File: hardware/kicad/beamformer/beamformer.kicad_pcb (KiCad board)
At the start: 2 copper layers, 96 parts, among them J1 SWD_HEADER, J2 USB_C_Receptacle_USB2.0_16P, U1 STM32H753ZITx, U2 USBLC6-2SC6, U3 TLC59116FIPWR, U4 ADAU7118ACPZRL, U5 MCP1826S-3302E/DB, U6 TLV75518PDBVR, U7 SN74AXC4T774PWR, Y1 16 MHz

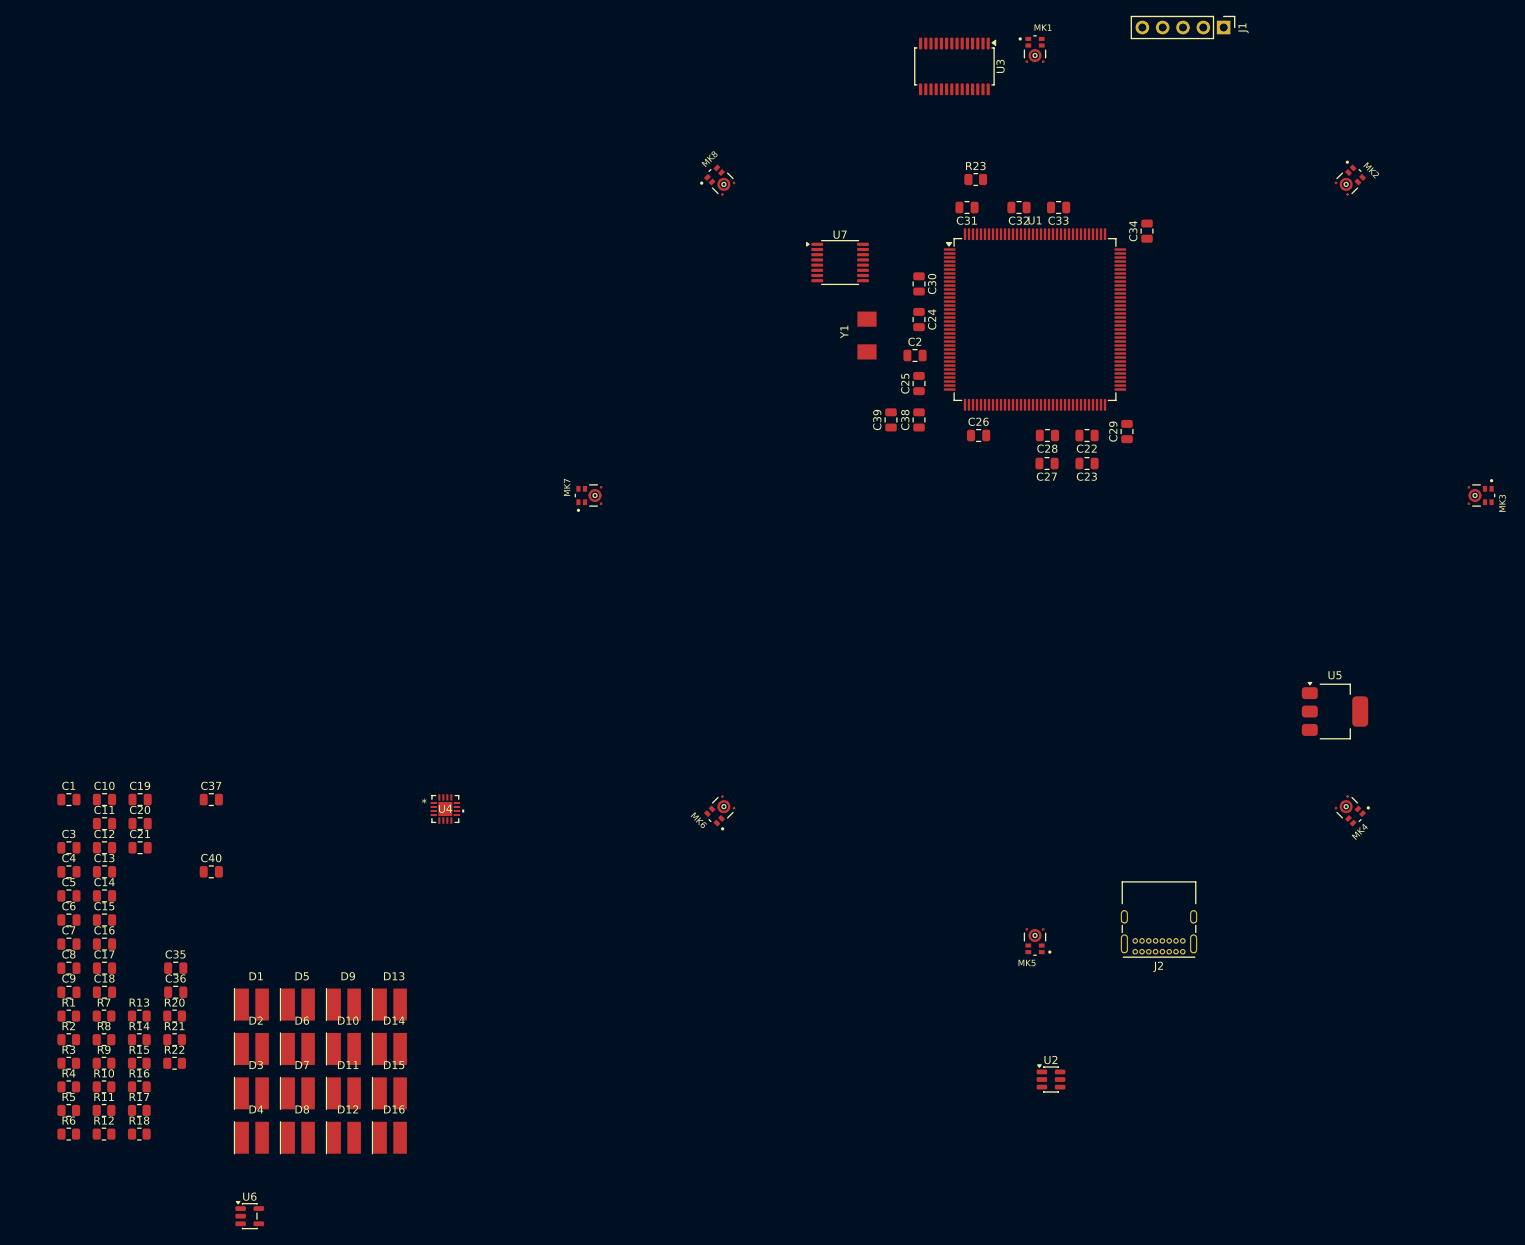
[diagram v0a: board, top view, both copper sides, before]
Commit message: pcb wiring started
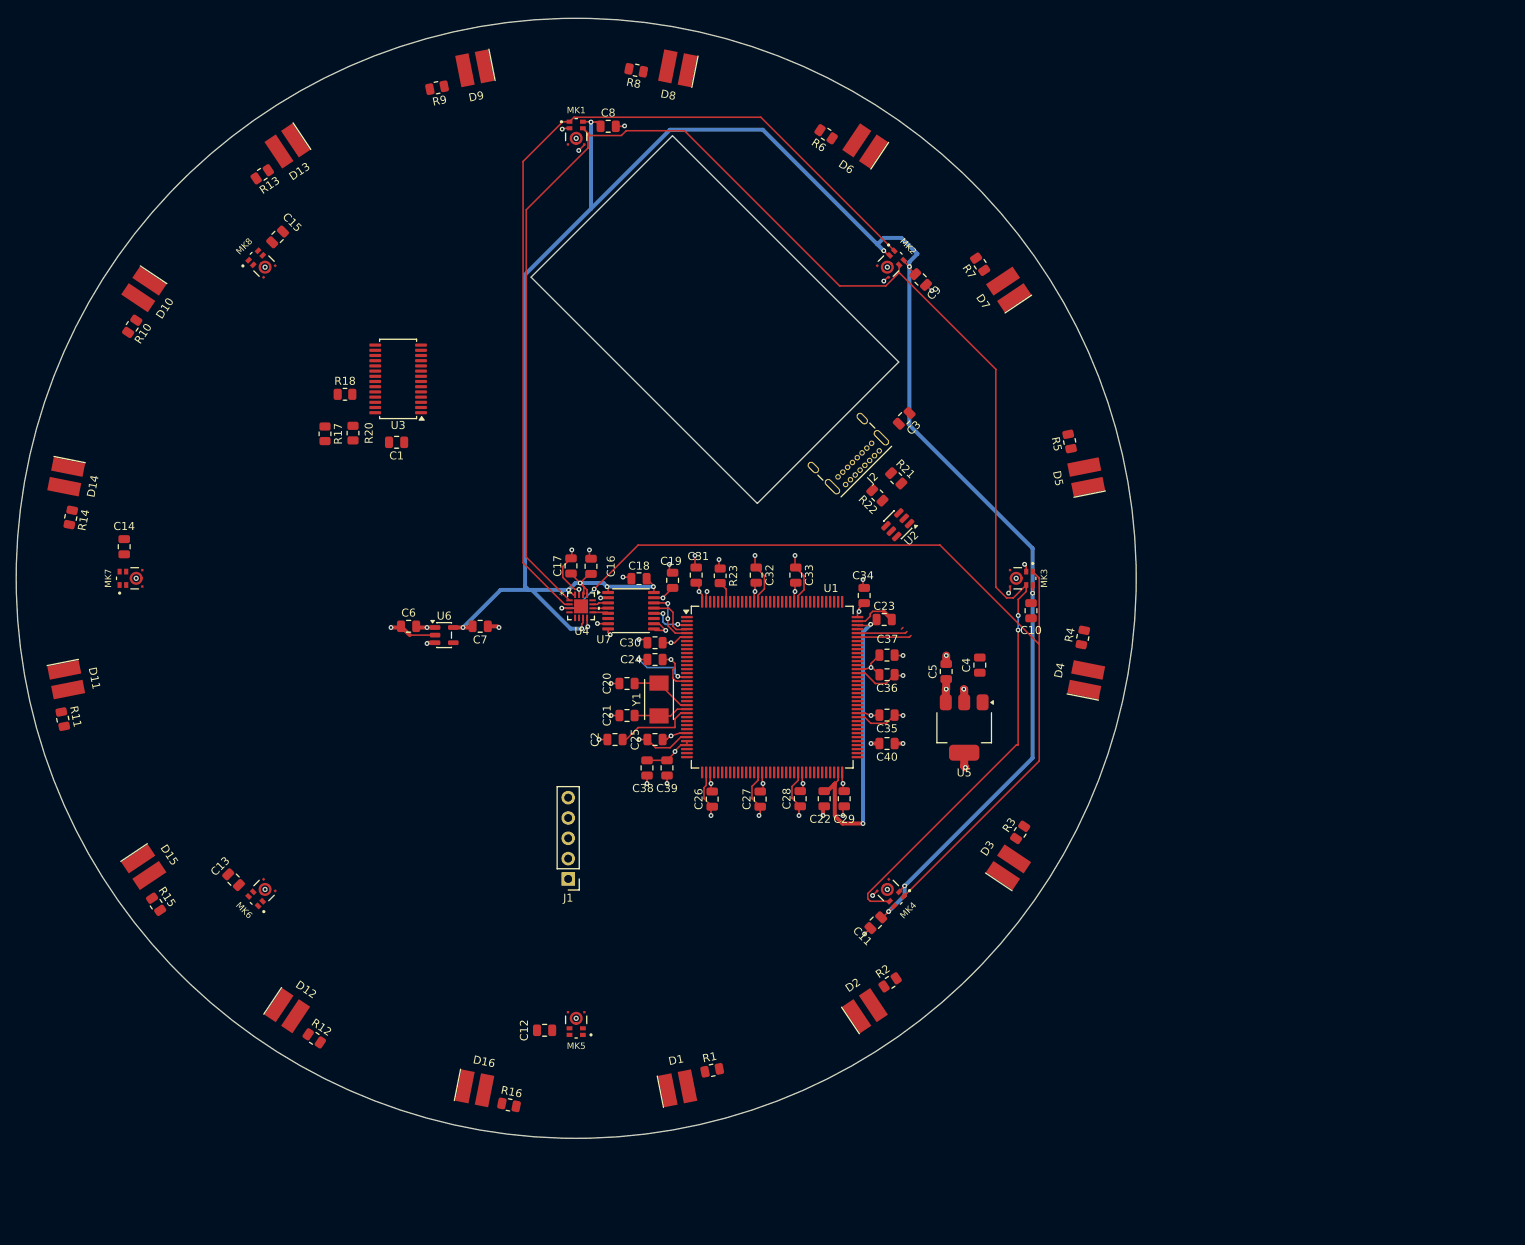
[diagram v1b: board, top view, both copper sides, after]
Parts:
- J2: footprint Connector_USB:USB_C_Receptacle_GCT_USB4085 -> Beamformer:USB_C_Receptacle_GCT_USB4085
- moved R6 156.8 mm to (130.4, 47.8), turned to 146.25 degrees
- moved R5 150.5 mm to (160.8, 86.2), turned to 101.25 degrees
- moved R7 144.3 mm to (149.6, 64.1), turned to 123.75 degrees
- moved D8 141.9 mm to (111.8, 39.6), turned to 168.75 degrees
- moved C9 138.8 mm to (142.2, 66.0), turned to -45 degrees
- moved R4 138.6 mm to (162.5, 110.7), turned to 78.75 degrees
- moved R8 138.2 mm to (106.6, 39.8), turned to 168.75 degrees
- moved J1 134.3 mm to (98.1, 140.9), turned to 180 degrees
- moved D7 134.1 mm to (153.2, 67.2), turned to 123.75 degrees
- moved D6 133.3 mm to (135.3, 49.3), turned to 146.25 degrees
- moved R9 128.9 mm to (81.8, 42.0), turned to -168.75 degrees
- moved C8 125.0 mm to (103.1, 46.8)
- moved R3 122.4 mm to (154.6, 135.1), turned to 56.25 degrees
- moved D4 118.9 mm to (162.9, 116.0), turned to 78.75 degrees
- moved D5 118.6 mm to (162.9, 90.7), turned to 101.25 degrees
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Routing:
- net +1V8: track 0.00 -> 271.1 mm, vias 0 -> 12
- net Net-(MK1-CLK): track 0.00 -> 214.3 mm, vias 0 -> 2
- net GND: track 0.00 -> 119.5 mm, vias 0 -> 47
- net Net-(MK3-DATA): track 0.00 -> 117.0 mm, vias 0 -> 2
- net Net-(MK1-DATA): track 0.00 -> 113.7 mm
- net +3V3: track 0.00 -> 58.0 mm, vias 0 -> 20
- net Net-(C22-Pad1): track 0.00 -> 38.3 mm, vias 0 -> 2
- net /NRST: track 0.00 -> 10.0 mm
- net Net-(U1-PH0): track 0.00 -> 7.71 mm
- net Net-(U1-PE6): track 0.00 -> 7.31 mm, vias 0 -> 2
- net Net-(U1-PH1): track 0.00 -> 6.91 mm
- net Net-(U1-PA11): track 0.00 -> 6.77 mm
- net Net-(U1-PA12): track 0.00 -> 6.27 mm
- net Net-(U1-PE5): track 0.00 -> 6.06 mm
- net Net-(U1-PE4): track 0.00 -> 5.33 mm, vias 0 -> 2
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- added copper zone on In2.Cu, net +3V3
- added copper zone on In1.Cu, net GND
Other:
- board outline added: 140 x 140 mm
- copper layers 2 -> 4

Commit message: PCB complete
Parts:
- added J3: Audio/UART Header, Connector_PinHeader_2.54mm:PinHeader_1x06_P2.54mm_Vertical, F.Cu at (93.4, 108.7)
- added TP1: GND, TestPoint:TestPoint_Pad_D1.5mm, F.Cu at (99.2, 96.0)
- added TP10: +1V8, TestPoint:TestPoint_Pad_D1.5mm, F.Cu at (88.0, 106.4)
- added TP11: +3V3, TestPoint:TestPoint_Pad_D1.5mm, F.Cu at (144.6, 76.4)
- added TP12: +5V, TestPoint:TestPoint_Pad_D1.5mm, F.Cu at (140.8, 81.4)
- added TP13: GND, TestPoint:TestPoint_Pad_D1.5mm, F.Cu at (142.6, 79.2)
- added TP2: PDM_DAT0, TestPoint:TestPoint_Pad_D1.5mm, F.Cu at (89.0, 98.2)
- added TP3: PDM_DAT1, TestPoint:TestPoint_Pad_D1.5mm, F.Cu at (106.6, 99.2)
- added TP4: PDM_CLK0, TestPoint:TestPoint_Pad_D1.5mm, F.Cu at (90.6, 95.4)
- added TP5: GND, TestPoint:TestPoint_Pad_D1.5mm, F.Cu at (99.4, 117.6)
- added TP6: PDM_DAT2, TestPoint:TestPoint_Pad_D1.5mm, F.Cu at (98.0, 111.0)
- added TP7: PDM_DAT3, TestPoint:TestPoint_Pad_D1.5mm, F.Cu at (91.8, 104.4)
- added TP8: PDM_CLK1, TestPoint:TestPoint_Pad_D1.5mm, F.Cu at (96.0, 124.8)
- added TP9: GND, TestPoint:TestPoint_Pad_D1.5mm, F.Cu at (86.8, 102.0)
- J2: value USB_C_Receptacle_USB2.0_16P -> USB4145-03-0170-C; footprint Beamformer:USB_C_Receptacle_GCT_USB4085 -> Beamformer:CONN_USB4145-03-0230-C_GCT
- moved J1 31.2 mm to (129.0, 136.2), turned to -90 degrees
- moved C3 13.2 mm to (127.3, 86.1), turned to -45 degrees
- moved R22 11.8 mm to (129.0, 84.2)
- moved J2 3.47 mm to (133.6, 87.9), turned to 45 degrees
- moved R17 3.35 mm to (70.2, 83.0), turned to 180 degrees
- moved C1 2.76 mm to (74.0, 85.8), turned to 90 degrees
- moved R20 1.05 mm to (70.2, 85.2), turned to 0 degrees
- moved R21 0.95 mm to (138.2, 90.8)
- moved C4 0.65 mm to (149.6, 114.8)
- moved C15 0.51 mm to (62.0, 60.2)
- moved U4 0.35 mm to (99.4, 106.8)
- moved C13 0.32 mm to (56.0, 141.0)
- moved R18 0.26 mm to (70.2, 80.6)
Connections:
- net Net-(U4-BCLK) renamed /BCLCK
- net Net-(U4-FSYNC) renamed /FSYNC
- net Net-(U4-SDATA) renamed /SDATA
- C3 pad 1: +5V -> GND
- C3 pad 2: GND -> +5V
- R21 pad 1: Net-(J2-CC1) -> Net-(J2-CC2)
- R22 pad 1: GND -> Net-(J2-CC1)
- R22 pad 2: Net-(J2-CC2) -> GND
- U1 pad 69: unconnected-(U1-PB10-Pad69) -> /TX
- U1 pad 70: unconnected-(U1-PB11-Pad70) -> /RX
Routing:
- net +5V: track 0.00 -> 544.7 mm, vias 0 -> 24
- net +1V8: track 271.1 -> 512.6 mm, vias 12 -> 20
- net Net-(MK5-CLK): track 0.00 -> 202.1 mm
- net Net-(D4-K): track 0.00 -> 152.2 mm, vias 0 -> 2
- net Net-(D3-K): track 0.00 -> 130.2 mm, vias 0 -> 2
- net Net-(D5-K): track 0.00 -> 129.1 mm
- net Net-(MK7-DATA): track 0.00 -> 121.1 mm, vias 0 -> 4
- net Net-(D2-K): track 0.00 -> 113.5 mm, vias 0 -> 2
- net Net-(MK5-DATA): track 0.00 -> 106.8 mm
- net Net-(D7-K): track 0.00 -> 105.5 mm
- net Net-(D1-K): track 0.00 -> 104.8 mm, vias 0 -> 2
- net Net-(D16-K): track 0.00 -> 100.7 mm, vias 0 -> 4
- net Net-(D12-K): track 0.00 -> 96.6 mm, vias 0 -> 4
- net Net-(D6-K): track 0.00 -> 80.8 mm
- net Net-(D15-K): track 0.00 -> 77.3 mm, vias 0 -> 2
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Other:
- outline, holes or cut-outs redrawn

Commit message: Added mounting holes tp pcb
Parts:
- added H1: MountingHole_3.2mm_M3, MountingHole:MountingHole_3.2mm_M3, F.Cu at (123.5, 69.8)
- added H2: MountingHole_3.2mm_M3, MountingHole:MountingHole_3.2mm_M3, F.Cu at (57.9, 99.0)
- added H3: MountingHole_3.2mm_M3, MountingHole:MountingHole_3.2mm_M3, F.Cu at (116.0, 141.3)
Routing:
- net GND: vias 88 -> 92
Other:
- board text added: "3V3"
- board text added: "BCLK"
- board text added: "FS"
- board text added: "GND"
- board text added: "NRST"
- board text added: "RX"
- board text added: "SDATA"
- board text added: "SWCLK"
- board text added: "SWDIO"
- board text added: "TX"
